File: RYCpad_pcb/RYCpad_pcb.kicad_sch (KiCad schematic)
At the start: 63 parts, among them J1 USB_C_Receptacle_USB2.0, J2 AVR ISP, K1 KEYSW, K10 KEYSW, K11 KEYSW, K12 KEYSW, K13 KEYSW, K14 KEYSW, K15 KEYSW, K16 KEYSW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

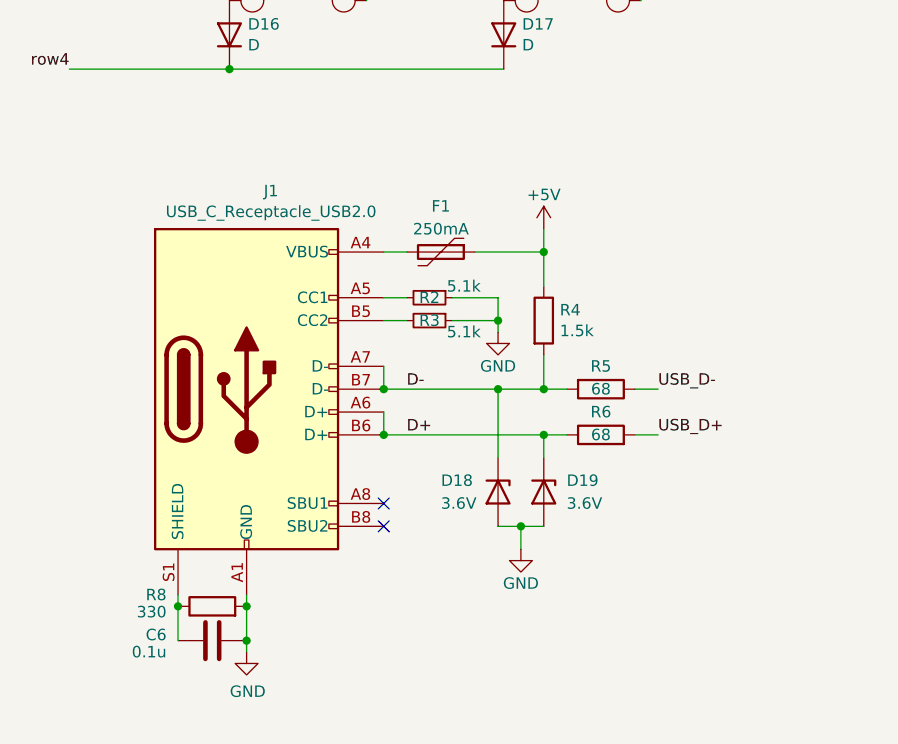
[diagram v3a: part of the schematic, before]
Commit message: revise usb shield strategy
- now shorted to ground
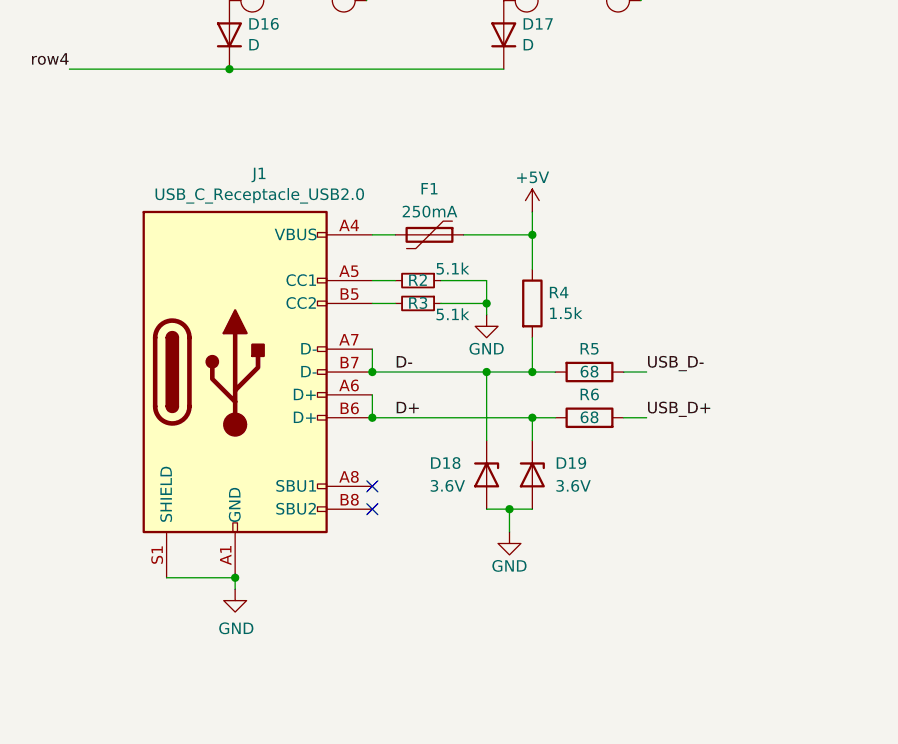
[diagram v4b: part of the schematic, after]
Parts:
- removed C6: 0.1u, Capacitor_THT:C_Disc_D4.3mm_W1.9mm_P5.00mm, symbol Device:C
- removed R8: 330, Resistor_THT:R_Axial_DIN0204_L3.6mm_D1.6mm_P5.08mm_Horizontal, symbol Device:R
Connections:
- net GND: now also J1.S1 (SHIELD)
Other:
- moved on the sheet: D18, D19, F1, J1, R2, R3, R4, R5, R6

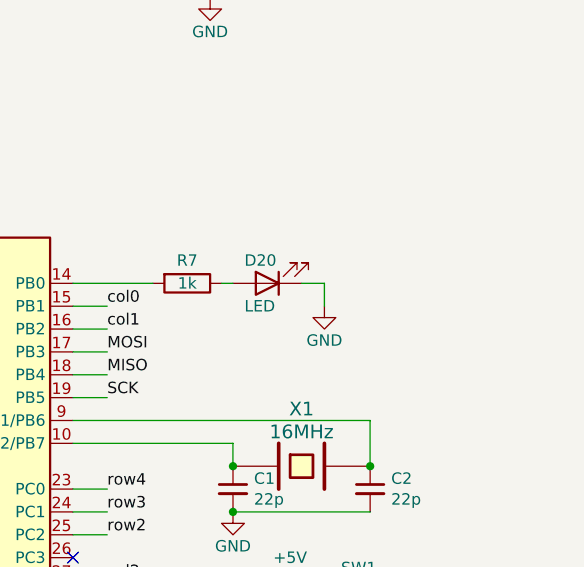
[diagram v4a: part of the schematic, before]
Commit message: minor routing changes, add suggested led
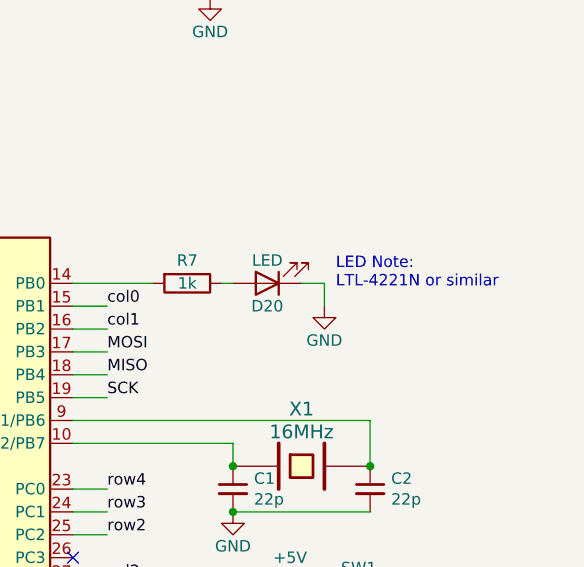
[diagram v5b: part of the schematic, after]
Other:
- note added: "LED Note: LTL-4221N or similar"
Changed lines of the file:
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@@
     (stroke (width 0) (type default) (color 0 0 0 0))
+  )
+  (text "LED Note:\nLTL-4221N or similar" (at 246.38 81.915 0)
+    (effects (font (size 1.27 1.27)) (justify left bottom))
   )
   (label "D-" (at 88.9 154.94 0)
@@
   (symbol (lib_id "Device:LED") (at 238.76 81.28 180) (unit 1)
     (in_bom yes) (on_board yes)
-    (property "Reference" "D20" (id 0) (at 236.22 78.74 0)
-      (effects (font (size 1.27 1.27)) (justify right))
-    )
-    (property "Value" "LED" (id 1) (at 236.22 83.82 0)
-      (effects (font (size 1.27 1.27)) (justify right))
-    )
+    (property "Reference" "D20" (id 0) (at 238.76 83.82 0))
+    (property "Value" "LED" (id 1) (at 238.76 78.74 0))
     (property "Footprint" "LED_THT:LED_D3.0mm" (id 2) (at 238.76 81.28 0)
       (effects (font (size 1.27 1.27)) hide)

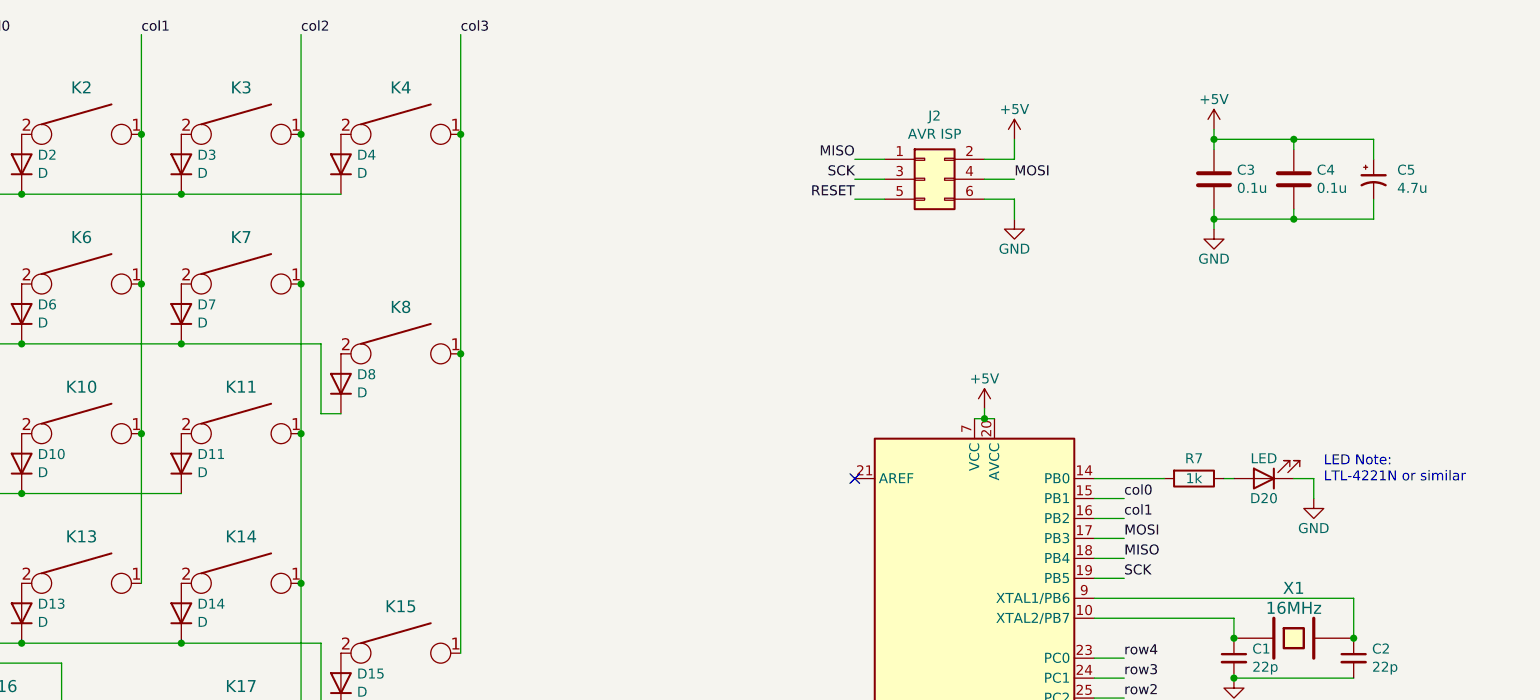
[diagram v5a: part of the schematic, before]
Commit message: update LED pin
- QMK supports hardware PWM on pin PB1 and PB2 for backlight dimming.
  The hope is that hardware PWM dimming can be exploited for the
  indicator LED, which mitigates any issues related to excessive LED
  brightness.
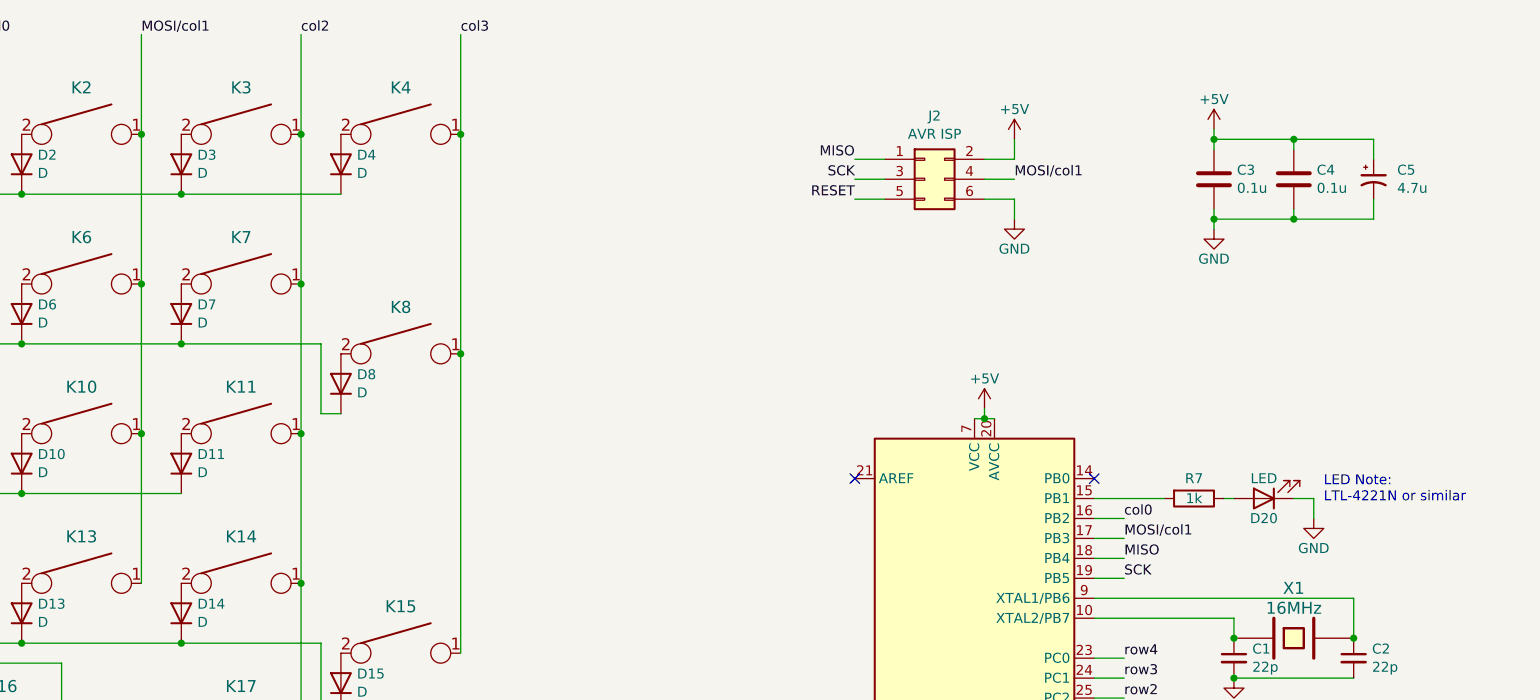
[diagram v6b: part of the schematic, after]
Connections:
- net col0: now also U1.16 (PB2); no longer U1.15 (PB1)
- net at U1.14 (PB0): no longer R7.2
- net MOSI renamed MOSI/col1
- net MOSI/col1: now also K10.1, K13.1, K2.1, K6.1
- removed net col1: K10.1, K13.1, K2.1, K6.1, U1.16 (PB2)
- new net: R7.2, U1.15 (PB1)
- no-connect marks 7 -> 8
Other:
- moved on the sheet: D20, R7
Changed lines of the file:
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@@
   (no_connect (at 86.36 167.64))
   (no_connect (at 186.69 81.28))
+  (no_connect (at 217.17 81.28))
   (no_connect (at 217.17 134.62))
   (wire (pts (xy 99.06 154.94) (xy 104.14 154.94))
@@
     (stroke (width 0) (type default) (color 0 0 0 0))
   )
-  (wire (pts (xy 217.17 81.28) (xy 226.06 81.28))
-    (stroke (width 0) (type default) (color 0 0 0 0))
-  )
   (wire (pts (xy 217.17 91.44) (xy 220.98 91.44))
     (stroke (width 0) (type default) (color 0 0 0 0))
@@
     (stroke (width 0) (type default) (color 0 0 0 0))
   )
-  (wire (pts (xy 217.17 83.82) (xy 220.98 83.82))
-    (stroke (width 0) (type default) (color 0 0 0 0))
-  )
-  (wire (pts (xy 233.68 81.28) (xy 234.95 81.28))
+  (wire (pts (xy 233.68 83.82) (xy 234.95 83.82))
     (stroke (width 0) (type default) (color 0 0 0 0))
   )
@@
     (stroke (width 0) (type default) (color 0 0 0 0))
   )
-  (wire (pts (xy 242.57 81.28) (xy 245.11 81.28))
+  (wire (pts (xy 242.57 83.82) (xy 245.11 83.82))
     (stroke (width 0) (type default) (color 0 0 0 0))
   )
@@
     (stroke (width 0) (type default) (color 0 0 0 0))
   )
-  (wire (pts (xy 245.11 81.28) (xy 245.11 83.82))
+  (wire (pts (xy 245.11 83.82) (xy 245.11 86.36))
     (stroke (width 0) (type default) (color 0 0 0 0))
   )
@@
     (stroke (width 0) (type default) (color 0 0 0 0))
   )
+  (wire (pts (xy 217.17 83.82) (xy 226.06 83.82))
+    (stroke (width 0) (type default) (color 0 0 0 0))
+  )
   (wire (pts (xy 231.14 116.84) (xy 231.14 119.38))
     (stroke (width 0) (type default) (color 0 0 0 0))
@@
     (stroke (width 0) (type default) (color 0 0 0 0))
   )
-  (text "LED Note:\nLTL-4221N or similar" (at 246.38 81.915 0)
+  (text "LED Note:\nLTL-4221N or similar" (at 246.38 84.455 0)
     (effects (font (size 1.27 1.27)) (justify left bottom))
   )
@@
     (effects (font (size 1.27 1.27)) (justify left bottom))
   )
-  (label "col0" (at 220.98 83.82 0)
-    (effects (font (size 1.27 1.27)) (justify left bottom))
-  )
   (label "RESET" (at 220.98 119.38 0)
     (effects (font (size 1.27 1.27)) (justify left bottom))
   )
-  (label "col1" (at 95.885 24.765 0)
+  (label "MOSI{slash}col1" (at 95.885 24.765 0)
     (effects (font (size 1.27 1.27)) (justify left bottom))
   )
@@
     (effects (font (size 1.27 1.27)) (justify left bottom))
   )
-  (label "MOSI" (at 220.98 88.9 0)
+  (label "MOSI{slash}col1" (at 220.98 88.9 0)
     (effects (font (size 1.27 1.27)) (justify left bottom))
   )
@@
     (effects (font (size 1.27 1.27)) (justify left bottom))
   )
+  (label "MOSI{slash}col1" (at 207.01 43.18 0)
+    (effects (font (size 1.27 1.27)) (justify left bottom))
+  )
   (label "row1" (at 52.705 64.135 180)
     (effects (font (size 1.27 1.27)) (justify right bottom))
@@
     (effects (font (size 1.27 1.27)) (justify left bottom))
   )
-  (label "col1" (at 220.98 86.36 0)
+  (label "col0" (at 220.98 86.36 0)
     (effects (font (size 1.27 1.27)) (justify left bottom))
   )
   (label "col3" (at 136.525 24.765 0)
-    (effects (font (size 1.27 1.27)) (justify left bottom))
-  )
-  (label "MOSI" (at 207.01 43.18 0)
     (effects (font (size 1.27 1.27)) (justify left bottom))
   )
@@
     (pin "2")
   )
-  (symbol (lib_id "Device:LED") (at 238.76 81.28 180) (unit 1)
-    (in_bom yes) (on_board yes)
-    (property "Reference" "D20" (id 0) (at 238.76 83.82 0))
-    (property "Value" "LED" (id 1) (at 238.76 78.74 0))
-    (property "Footprint" "LED_THT:LED_D3.0mm" (id 2) (at 238.76 81.28 0)
-      (effects (font (size 1.27 1.27)) hide)
-    )
-    (property "Datasheet" "~" (id 3) (at 238.76 81.28 0)
-      (effects (font (size 1.27 1.27)) hide)
-    )
-    (pin "1")
-    (pin "2")
-  )
-  (symbol (lib_id "Device:R") (at 229.87 81.28 270) (unit 1)
-    (in_bom yes) (on_board yes)
-    (property "Reference" "R7" (id 0) (at 229.87 78.74 90))
-    (property "Value" "1k" (id 1) (at 229.87 81.28 90))
-    (property "Footprint" "Resistor_THT:R_Axial_DIN0204_L3.6mm_D1.6mm_P5.08mm_Horizontal" (id 2) (at 229.87 79.502 90)
-      (effects (font (size 1.27 1.27)) hide)
-    )
-    (property "Datasheet" "~" (id 3) (at 229.87 81.28 0)
+  (symbol (lib_id "Device:LED") (at 238.76 83.82 180) (unit 1)
+    (in_bom yes) (on_board yes)
+    (property "Reference" "D20" (id 0) (at 238.76 86.36 0))
+    (property "Value" "LED" (id 1) (at 238.76 81.28 0))
+    (property "Footprint" "LED_THT:LED_D3.0mm" (id 2) (at 238.76 83.82 0)
+      (effects (font (size 1.27 1.27)) hide)
+    )
+    (property "Datasheet" "~" (id 3) (at 238.76 83.82 0)
+      (effects (font (size 1.27 1.27)) hide)
+    )
+    (pin "1")
+    (pin "2")
+  )
+  (symbol (lib_id "Device:R") (at 229.87 83.82 270) (unit 1)
+    (in_bom yes) (on_board yes)
+    (property "Reference" "R7" (id 0) (at 229.87 81.28 90))
+    (property "Value" "1k" (id 1) (at 229.87 83.82 90))
+    (property "Footprint" "Resistor_THT:R_Axial_DIN0204_L3.6mm_D1.6mm_P5.08mm_Horizontal" (id 2) (at 229.87 82.042 90)
+      (effects (font (size 1.27 1.27)) hide)
+    )
+    (property "Datasheet" "~" (id 3) (at 229.87 83.82 0)
       (effects (font (size 1.27 1.27)) hide)
     )
@@
     (pin "1")
   )
-  (symbol (lib_id "power:GND") (at 245.11 83.82 0) (unit 1)
-    (in_bom yes) (on_board yes)
-    (property "Reference" "#PWR0104" (id 0) (at 245.11 90.17 0)
-      (effects (font (size 1.27 1.27)) hide)
-    )
-    (property "Value" "GND" (id 1) (at 245.11 87.63 0))
-    (property "Footprint" "" (id 2) (at 245.11 83.82 0)
-      (effects (font (size 1.27 1.27)) hide)
-    )
-    (property "Datasheet" "" (id 3) (at 245.11 83.82 0)
-      (effects (font (size 1.27 1.27)) hide)
-    )
+  (symbol (lib_id "power:GND") (at 245.11 86.36 0) (unit 1)
+    (in_bom yes) (on_board yes)
+    (property "Reference" "#PWR0104" (id 0) (at 245.11 92.71 0)
+      (effects (font (size 1.27 1.27)) hide)
+    )
+    (property "Value" "GND" (id 1) (at 245.11 90.17 0))
+    (property "Footprint" "" (id 2) (at 245.11 86.36 0)
+      (effects (font (size 1.27 1.27)) hide)
+    )
+    (property "Datasheet" "" (id 3) (at 245.11 86.36 0)
+      (effects (font (size 1.27 1.27)) hide)
+    )
